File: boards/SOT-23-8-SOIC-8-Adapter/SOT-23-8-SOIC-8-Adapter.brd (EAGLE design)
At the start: 12.7 x 12.7 mm, 5 parts, among them J1 PINHD-1X4, J2 PINHD-1X4, Q1 LTC4365, Q2 IRLML2060TRPBF, Q3 IRLML2060TRPBF

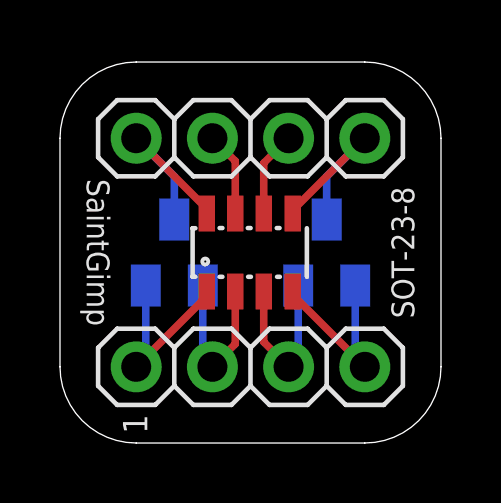
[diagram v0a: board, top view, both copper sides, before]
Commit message: Fixed SOT-23-8 adapter to have right footprint, and added SOIC-8
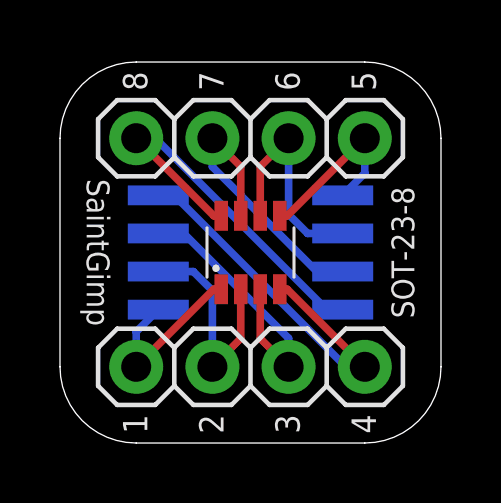
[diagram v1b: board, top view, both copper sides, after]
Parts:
- removed Q2, Q3: IRLML2060TRPBF, SaintGimp:SOT-23-3
- added U$1: DUMMY1, SaintGimp:SOIC-08
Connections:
- net 1-1: now also U$1.1; no longer Q2.2
- net 1-2: now also U$1.2; no longer Q2.1
- net 1-3: now also U$1.3; no longer Q3.2
- net 1-4: now also U$1.4; no longer Q3.1
- net 2-1: now also U$1.8; no longer Q2.3
- net 2-2: now also U$1.7
- net 2-3: now also U$1.6
- net 2-4: now also U$1.5; no longer Q3.3
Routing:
- net 2-2: track 2.83 -> 9.72 mm
- net 1-4: track 6.35 -> 13.2 mm
- net 2-1: track 6.70 -> 13.2 mm
- net 2-3: track 2.85 -> 7.58 mm
- net 1-3: track 5.70 -> 9.72 mm
- net 1-2: track 5.67 -> 7.58 mm
- net 2-4: track 6.74 -> 6.12 mm
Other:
- board text added: "2"
- board text added: "3"
- board text added: "4"
- board text added: "5"
- board text added: "6"
- board text added: "7"
- board text added: "8"
- board text added: "SOIC-08"
- board text removed: "SOT-23"
